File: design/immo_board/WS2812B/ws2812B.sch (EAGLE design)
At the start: 11 parts

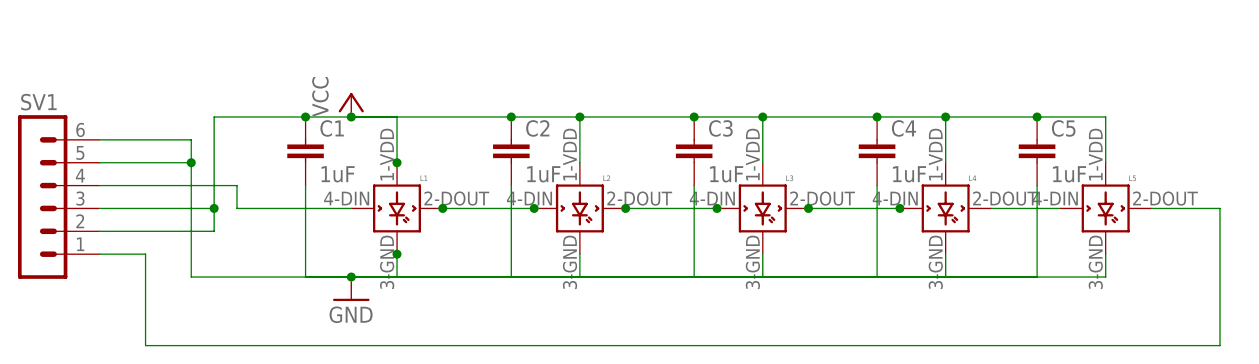
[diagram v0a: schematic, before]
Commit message: Fix board and electric scheme. Add capacitors.
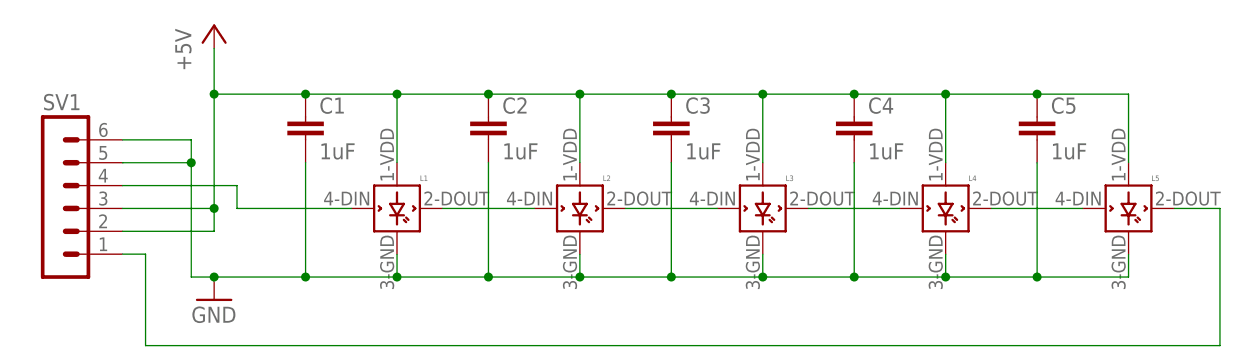
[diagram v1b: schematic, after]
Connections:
- net VCC renamed +5V
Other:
- moved on the sheet: C1, C2, C3, C4, C5, L5, SV1
